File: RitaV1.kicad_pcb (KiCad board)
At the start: 2 copper layers, 115.6 x 91.4 mm, 25 parts, among them J100 VCC SUPPLY, J200 LORA, J201 GPS, J202 ANEM, J203 MICROSD, J300 BATERIA MOTOR, J301 CORRIENTE_ADC, U100 YAAJ_DCDC_StepDown_LM2596, U101 LM7805_TO220, U200 BP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

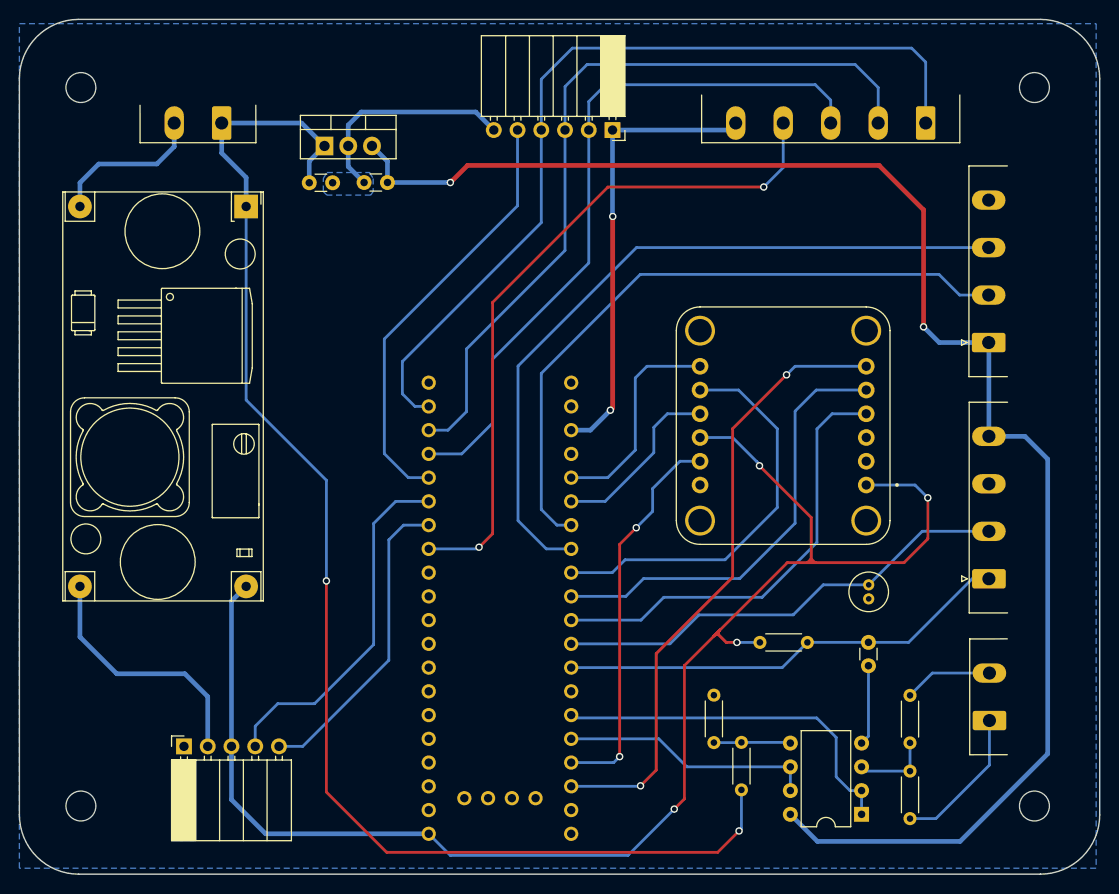
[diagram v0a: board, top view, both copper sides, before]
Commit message: Cambios: Lora comunicacion UART, comunicacion I2C para analizer y Atmega
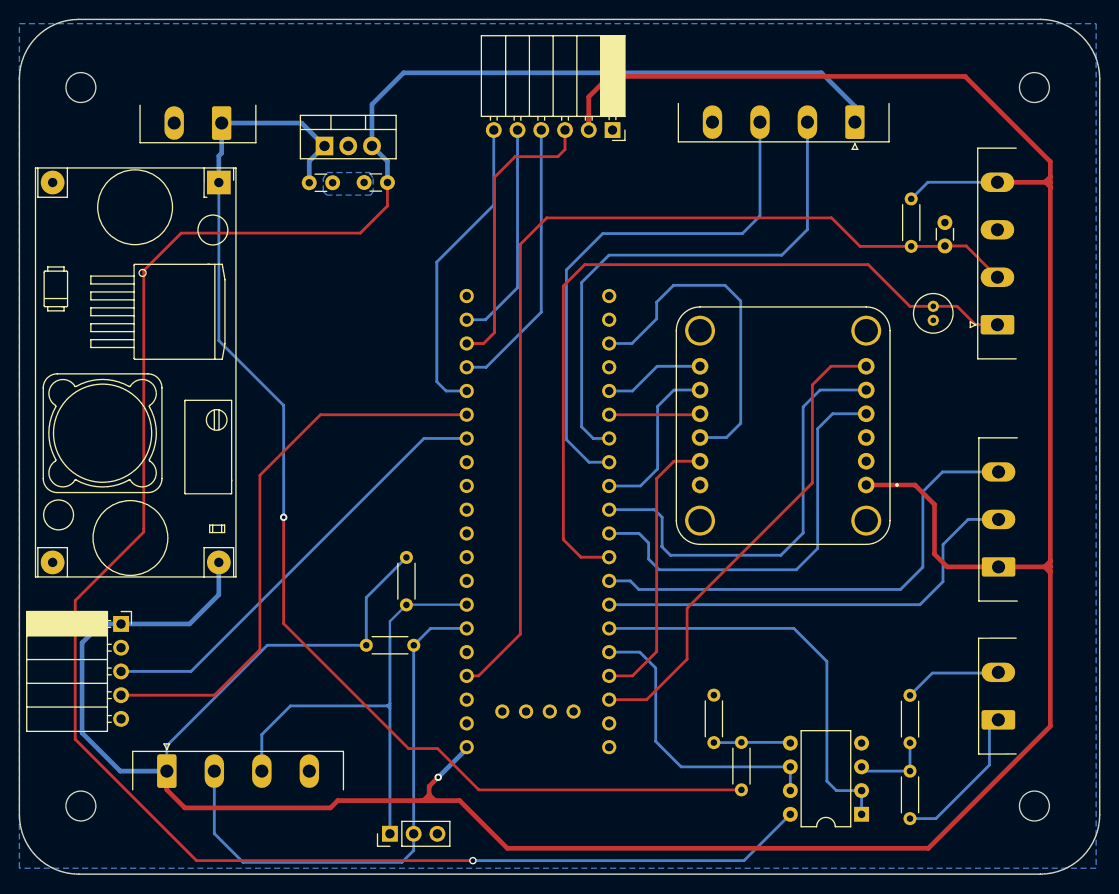
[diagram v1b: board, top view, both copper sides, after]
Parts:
- added J204: ATMEGA, Connector_Phoenix_MSTB:PhoenixContact_MSTBA_2,5_4-G-5,08_1x04_P5.08mm_Horizontal, F.Cu at (64.0, 114.7)
- added J205: LOGIC ANALIZER, Connector_PinHeader_2.54mm:PinHeader_1x03_P2.54mm_Vertical, F.Cu at (87.9, 121.4)
- added R200: 4k7, Resistor_THT:R_Axial_DIN0204_L3.6mm_D1.6mm_P5.08mm_Horizontal, F.Cu at (85.4, 101.2)
- added R201: 4k7, Resistor_THT:R_Axial_DIN0204_L3.6mm_D1.6mm_P5.08mm_Horizontal, F.Cu at (89.7, 91.8)
- J200: footprint Connector_Phoenix_MSTB:PhoenixContact_MSTBA_2,5_5-G-5,08_1x05_P5.08mm_Horizontal -> Connector_Phoenix_MSTB:PhoenixContact_MSTBA_2,5_3-G-5,08_1x03_P5.08mm_Horizontal
- moved R202 50.1 mm to (143.7, 53.5), turned to -90 degrees
- moved J200 48.1 mm to (153.0, 92.9), turned to 90 degrees
- moved C201 48.1 mm to (147.3, 56.0), turned to -90 degrees
- moved C200 30.6 mm to (146.0, 65.0)
- moved J301 27.6 mm to (137.6, 45.3), turned to 180 degrees
- moved J202 27.2 mm to (152.9, 67.0)
- moved J201 14.7 mm to (59.1, 99.0), turned to 0 degrees
- moved U200 10.1 mm to (105.6, 84.8)
- moved U100 3.89 mm to (69.6, 51.7)
- moved J300 0.96 mm to (153.0, 109.2)
- renumbered R200 to R202
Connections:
- J200 pad 1: /MCU/SCK_2 -> +3V3
- J200 pad 2: /MCU/MISO_2 -> /MCU/RX_LORA
- J200 pad 3: /MCU/MOSI_2 -> /MCU/TX_LORA
- J201 pad 1: unconnected-(J201-Pad1) -> +3V3
- J201 pad 3: +3V3 -> /MCU/TX_GPS
- J201 pad 5: /MCU/TX_GPS -> unconnected-(J201-Pad5)
- J202 pad 1: /MCU/ANEM_SPEED -> /MCU/ANEM_DIR
- J202 pad 2: /MCU/ANEM_DIR -> /MCU/ANEM_SPEED
- J202 pad 4: +5V -> +3V3
- J203 pad 1: +3V3 -> GND
- J203 pad 2: /MCU/MOSI_2 -> +3V3
- J203 pad 4: /MCU/SCK_2 -> /MCU/MOSI_2
- J203 pad 5: /MCU/CS_SD -> /MCU/SCK_2
- J203 pad 6: GND -> /MCU/CS_SD
- U200 pad PA11: /MCU/CS_LORA -> unconnected-(U200-PadPA11)
- U200 pad PA2: unconnected-(U200-PadPA2) -> /MCU/RX_LORA
- U200 pad PA3: /MCU/ANEM_SPEED -> /MCU/TX_LORA
- U200 pad PB6: unconnected-(U200-PadPB6) -> /MCU/SCL
- U200 pad PB7: unconnected-(U200-PadPB7) -> /MCU/SDA
- U200 pad PB9: unconnected-(U200-PadPB9) -> /MCU/ANEM_SPEED
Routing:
- net +3V3: track 210.8 -> 394.6 mm, vias 6 -> 1
- net GND: track 91.8 -> 16.1 mm
- net /MCU/CS_LORA: track 74.1 -> 0.00 mm, vias 2 -> 0
- net /MCU/SCK_2: track 92.8 -> 23.7 mm
- net +5V: track 166.3 -> 233.8 mm, vias 2 -> 1
- net /MCU/SDA: track 0.00 -> 58.2 mm
- net /MCU/ANEM_SPEED: track 48.6 -> 104.2 mm
- net /MCU/MISO_2: track 83.3 -> 30.9 mm
- net /MCU/TX_LORA: track 0.00 -> 52.0 mm
- net /MCU/SCL: track 0.00 -> 51.3 mm
- net /MCU/RX_LORA: track 0.00 -> 47.8 mm
- net /MCU/MOSI_2: track 76.6 -> 29.9 mm
- net /MCU/ANEM_DIR: track 49.7 -> 82.9 mm
- net /MCU/MOSI_1: track 43.3 -> 17.9 mm
- net C_MOTOR_2: track 79.1 -> 56.9 mm
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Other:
- board text added: "0.2000 mm / 0.2000 mm"
- board text added: "0.3000 mm"
- board text added: "1.6000 mm"
- board text added: "115.5700 mm x 91.4400 mm"
- board text added: "2"
- board text added: "BOARD CHARACTERISTICS"
- board text added: "Board Thickness:"
- board text added: "Board overall dimensions:"
- board text added: "Castellated pads:"
- board text added: "Copper Finish:"
- board text added: "Copper Layer Count:"
- board text added: "Edge card connectors:"
- board text added: "Impedance Control:"
- board text added: "Min hole diameter:"
- board text added: "Min track/spacing:"
- board text added: "No"
- board text added: "None"
- board text added: "Plated Board Edge:"
